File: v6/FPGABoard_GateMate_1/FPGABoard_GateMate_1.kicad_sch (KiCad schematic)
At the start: 0 parts

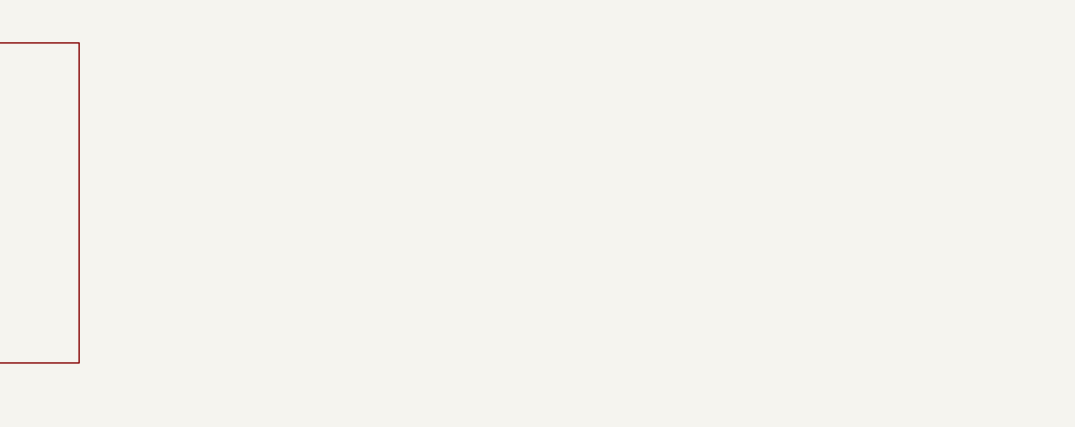
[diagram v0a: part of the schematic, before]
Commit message: Add comments for GateMAte board
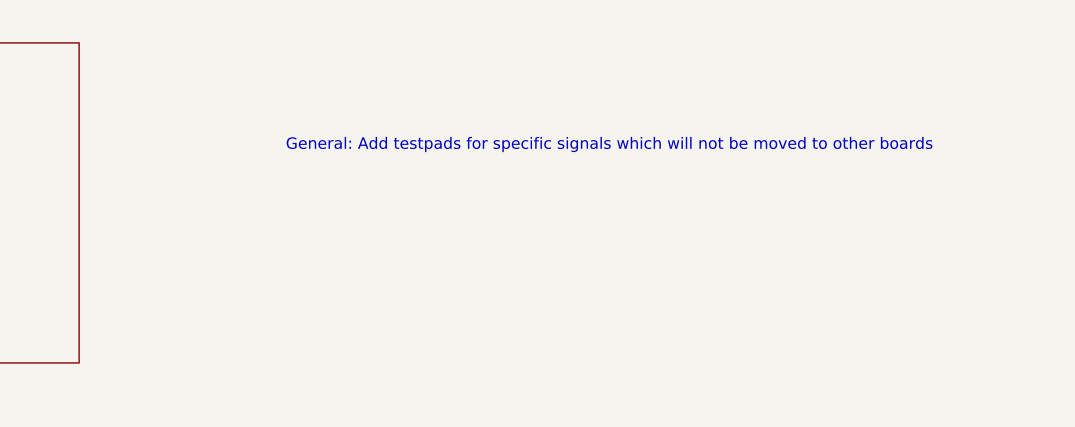
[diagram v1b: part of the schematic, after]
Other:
- note added: "General: Add testpads for specific signals which will not be moved to other boards"
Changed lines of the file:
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@@
 (kicad_sch
-	(version 20250114)
+	(version 20260306)
 	(generator "eeschema")
-	(generator_version "9.0")
+	(generator_version "10.0")
 	(paper "A4")
+	(text "General: Add testpads for specific signals which will not be moved to other boards"
+		(exclude_from_sim no)
+		(at 179.578 36.83 0)
+		(effects
+			(font
+				(size 1.27 1.27)
+			)
+		)
+	)
 	(text "V Outputs from MCU"
 		(exclude_from_sim no)
@@
 		)
 		(fill
-			(color 0 0 0 0.0000)
+			(color 0 0 0 0)
 		)
 		(property "Sheetname" "FPGA_Config"
 			(at 81.28 24.6884 0)
+			(show_name no)
+			(do_not_autoplace no)
 			(effects
 				(font
@@
 		(property "Sheetfile" "FPGA_Config.kicad_sch"
 			(at 81.28 61.5446 0)
+			(show_name no)
+			(do_not_autoplace no)
 			(effects
 				(font
@@
 		)
 		(fill
-			(color 0 0 0 0.0000)
+			(color 0 0 0 0)
 		)
 		(property "Sheetname" "FPGA_Power"
 			(at 97.79 85.6484 0)
+			(show_name no)
+			(do_not_autoplace no)
 			(effects
 				(font
@@
 		(property "Sheetfile" "FPGA_Power.kicad_sch"
 			(at 97.79 127.5846 0)
+			(show_name no)
+			(do_not_autoplace no)
 			(effects
 				(font
@@
 		)
 		(fill
-			(color 0 0 0 0.0000)
+			(color 0 0 0 0)
 		)
 		(property "Sheetname" "FPGA_IO_Banks"
 			(at 44.45 85.6484 0)
+			(show_name no)
+			(do_not_autoplace no)
 			(effects
 				(font
@@
 		(property "Sheetfile" "FPGA_IO_Banks.kicad_sch"
 			(at 44.45 127.5846 0)
+			(show_name no)
+			(do_not_autoplace no)
 			(effects
 				(font
@@
 		)
 		(fill
-			(color 0 0 0 0.0000)
+			(color 0 0 0 0)
 		)
 		(property "Sheetname" "Connectors"
 			(at 25.4 24.6884 0)
+			(show_name no)
+			(do_not_autoplace no)
 			(effects
 				(font
@@
 		(property "Sheetfile" "Connectors.kicad_sch"
 			(at 25.4 61.5446 0)
-			(effects
-				(font
+			(show_name no)
+			(do_not_autoplace no)
+			(effects
+				(font
